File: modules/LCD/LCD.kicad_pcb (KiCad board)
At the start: 2 copper layers, 82.5 x 40.6 mm, 8 parts, among them J1 Conn_01x10_Male, J2 Conn_01x10_Male

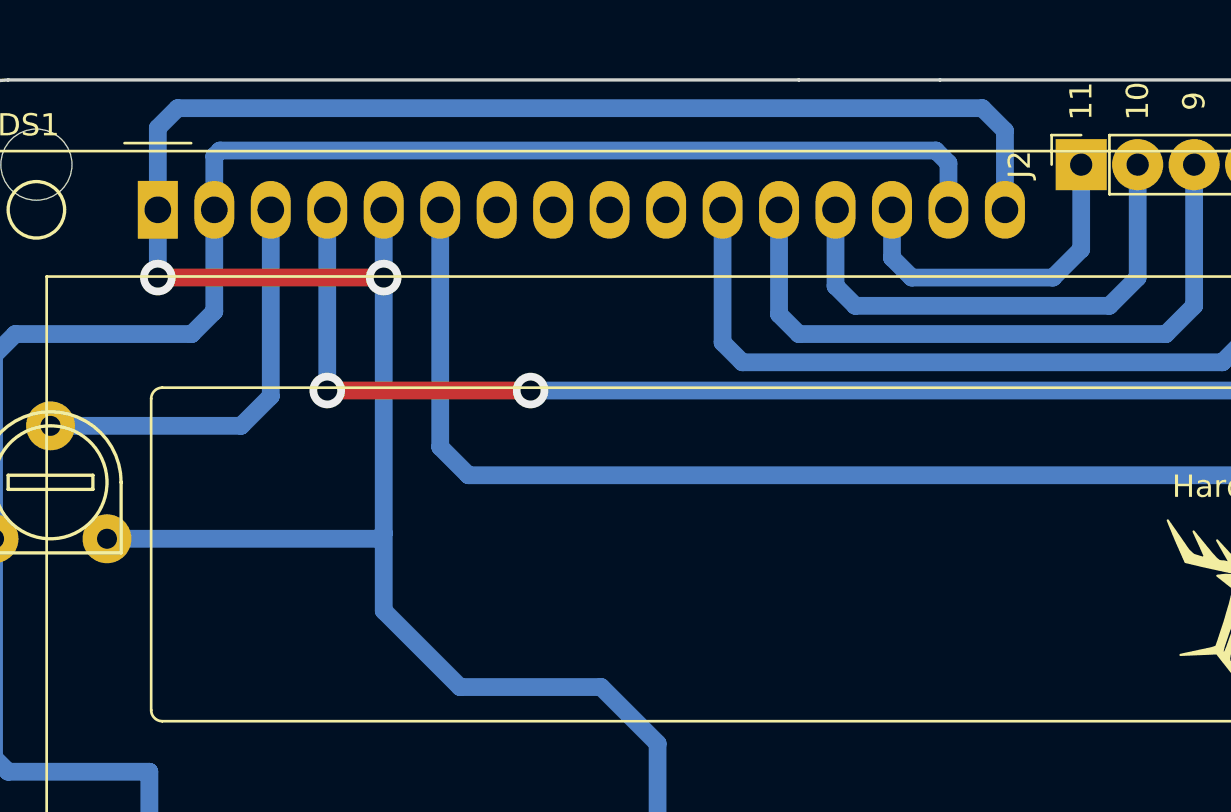
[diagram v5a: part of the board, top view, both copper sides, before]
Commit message: My LCD does not have LED resistor :( Add silk etc
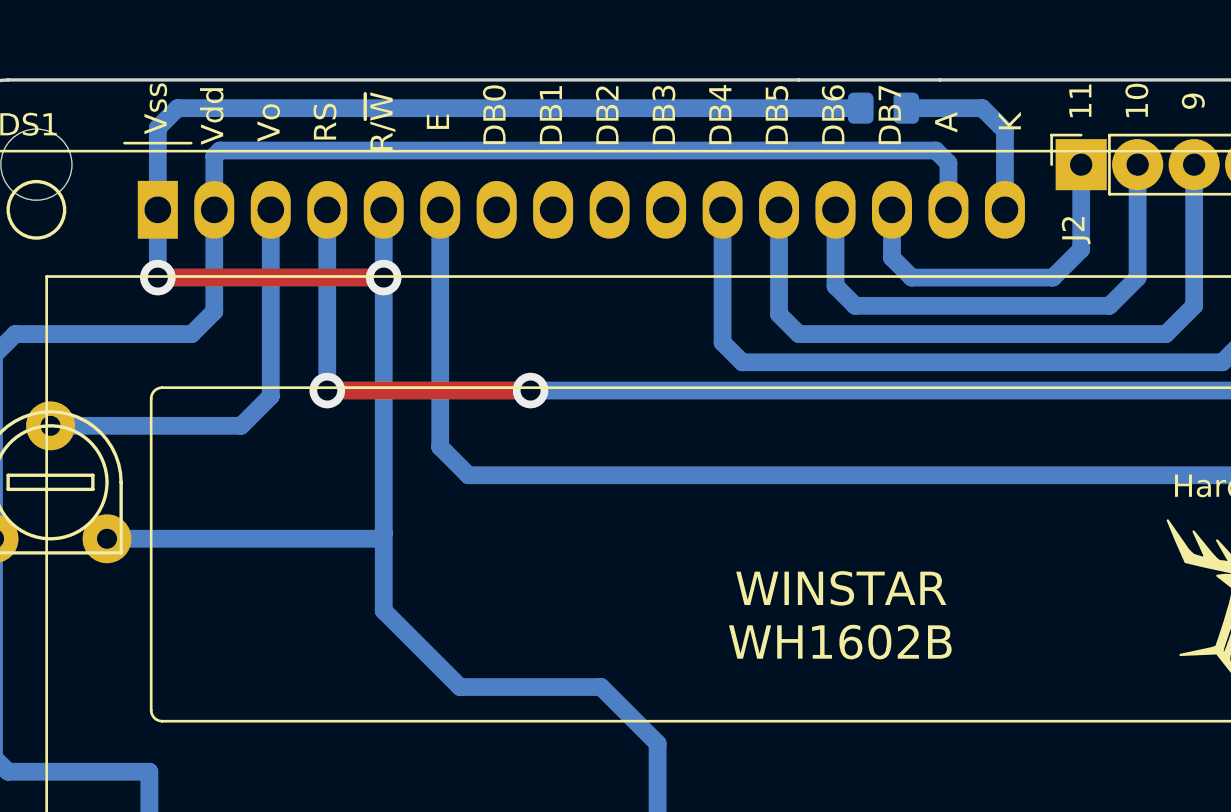
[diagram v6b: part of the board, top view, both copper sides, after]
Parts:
- added R1: 20, Resistor_SMD:R_0805_2012Metric_Pad1.15x1.40mm_HandSolder, B.Cu at (111.1, 26.7)
- DS1: value WC1602A -> WH1602B
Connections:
- DS1 pad 16: GND -> Net-(DS1-Pad16)
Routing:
- net GND: track 111.6 -> 101.2 mm
- net Net-(DS1-Pad16): track 0.00 -> 8.41 mm
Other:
- board text added: "A"
- board text added: "DB0"
- board text added: "DB1"
- board text added: "DB2"
- board text added: "DB3"
- board text added: "DB4"
- board text added: "DB5"
- board text added: "DB6"
- board text added: "DB7"
- board text added: "E"
- board text added: "K"
- board text added: "R/~W"
- board text added: "RS"
- board text added: "Vdd"
- board text added: "Vo"
- board text added: "Vss"
- board text added: "WINSTAR WH1602B"
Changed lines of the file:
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@@
   (general
     (thickness 1.6)
-    (drawings 37)
-    (tracks 74)
+    (drawings 54)
+    (tracks 75)
     (zones 0)
-    (modules 8)
-    (nets 26)
+    (modules 9)
+    (nets 27)
   )
   (page A4 portrait)
@@
   )
   (setup
-    (last_trace_width 0.25)
+    (last_trace_width 0.6)
     (user_trace_width 0.6)
     (user_trace_width 0.8)
@@
   (net 24 "Net-(DS1-Pad8)")
   (net 25 "Net-(DS1-Pad7)")
+  (net 26 "Net-(DS1-Pad16)")
   (net_class Default "Это класс цепей по умолчанию."
     (clearance 0.2)
@@
     (add_net GND)
     (add_net "Net-(DS1-Pad10)")
+    (add_net "Net-(DS1-Pad16)")
     (add_net "Net-(DS1-Pad3)")
     (add_net "Net-(DS1-Pad7)")
@@
     (descr "Through hole straight socket strip, 1x10, 2.54mm pitch, single row (from Kicad 4.0.7), script generated")
     (tags "Through hole socket strip THT 1x10 2.54mm single row")
-    (fp_text reference J2 (at 0 -2.77 90) (layer F.SilkS)
+    (fp_text reference J2 (at -2.8575 -0.3175 90) (layer F.SilkS)
       (effects (font (size 1 1) (thickness 0.15)))
     )
@@
       (effects (font (size 1 1) (thickness 0.15)))
     )
-    (fp_text value WC1602A (at -4.31 34.66) (layer F.Fab)
+    (fp_text value WH1602B (at -4.31 34.66) (layer F.Fab)
       (effects (font (size 1 1) (thickness 0.15)))
     )
@@
     (fp_circle (center 69.469 30.988) (end 70.231 32.004) (layer F.SilkS) (width 0.15))
     (pad 16 thru_hole oval (at 38.1 0) (size 1.8 2.6) (drill 1.2) (layers *.Cu *.Mask)
-      (net 10 GND))
+      (net 26 "Net-(DS1-Pad16)"))
     (pad 15 thru_hole oval (at 35.56 0) (size 1.8 2.6) (drill 1.2) (layers *.Cu *.Mask)
       (net 1 VCC))
@@
       (net 10 GND))
   )
+  (module Resistor_SMD:R_0805_2012Metric_Pad1.15x1.40mm_HandSolder (layer B.Cu)
+    (at 111.125 26.67 180)
+    (descr "Resistor SMD 0805 (2012 Metric), square (rectangular) end terminal, IPC_7351 nominal with elongated pad for handsoldering. (Body size source: https://docs.google.com/spreadsheets/d/1BsfQQcO9C6DZCsRaXUlFlo91Tg2WpOkGARC1WS5S8t0/edit?usp=sharing), generated with kicad-footprint-generator")
+    (tags "resistor handsolder")
+    (attr smd)
+    (fp_text reference R1 (at -3.175 0) (layer B.SilkS)
+      (effects (font (size 1 1) (thickness 0.15)) (justify mirror))
+    )
+    (fp_text value 20 (at 0 -1.65) (layer B.Fab)
+      (effects (font (size 1 1) (thickness 0.15)) (justify mirror))
+    )
+    (fp_line (start -1 -0.6) (end -1 0.6) (layer B.Fab) (width 0.1))
+    (fp_line (start -1 0.6) (end 1 0.6) (layer B.Fab) (width 0.1))
+    (fp_line (start 1 0.6) (end 1 -0.6) (layer B.Fab) (width 0.1))
+    (fp_line (start 1 -0.6) (end -1 -0.6) (layer B.Fab) (width 0.1))
+    (fp_line (start -0.261252 0.71) (end 0.261252 0.71) (layer B.SilkS) (width 0.12))
+    (fp_line (start -0.261252 -0.71) (end 0.261252 -0.71) (layer B.SilkS) (width 0.12))
+    (fp_line (start -1.85 -0.95) (end -1.85 0.95) (layer B.CrtYd) (width 0.05))
+    (fp_line (start -1.85 0.95) (end 1.85 0.95) (layer B.CrtYd) (width 0.05))
+    (fp_line (start 1.85 0.95) (end 1.85 -0.95) (layer B.CrtYd) (width 0.05))
+    (fp_line (start 1.85 -0.95) (end -1.85 -0.95) (layer B.CrtYd) (width 0.05))
+    (fp_text user %R (at 0 0) (layer B.Fab)
+      (effects (font (size 0.5 0.5) (thickness 0.08)) (justify mirror))
+    )
+    (pad 1 smd roundrect (at -1.025 0 180) (size 1.15 1.4) (layers B.Cu B.Paste B.Mask) (roundrect_rratio 0.217391)
+      (net 26 "Net-(DS1-Pad16)"))
+    (pad 2 smd roundrect (at 1.025 0 180) (size 1.15 1.4) (layers B.Cu B.Paste B.Mask) (roundrect_rratio 0.217391)
+      (net 10 GND))
+    (model ${KISYS3DMOD}/Resistor_SMD.3dshapes/R_0805_2012Metric.wrl
+      (at (xyz 0 0 0))
+      (scale (xyz 1 1 1))
+      (rotate (xyz 0 0 0))
+    )
+  )
+  (gr_text K (at 116.84 27.305 90) (layer F.SilkS)
+    (effects (font (size 1 1) (thickness 0.15)))
+  )
+  (gr_text A (at 113.9825 27.305 90) (layer F.SilkS)
+    (effects (font (size 1 1) (thickness 0.15)))
+  )
+  (gr_text DB7 (at 111.4425 26.9875 90) (layer F.SilkS)
+    (effects (font (size 1 1) (thickness 0.15)))
+  )
+  (gr_text DB6 (at 108.9025 26.9875 90) (layer F.SilkS)
+    (effects (font (size 1 1) (thickness 0.15)))
+  )
+  (gr_text DB5 (at 106.3625 26.9875 90) (layer F.SilkS)
+    (effects (font (size 1 1) (thickness 0.15)))
+  )
+  (gr_text DB4 (at 103.8225 26.9875 90) (layer F.SilkS)
+    (effects (font (size 1 1) (thickness 0.15)))
+  )
+  (gr_text DB3 (at 101.2825 26.9875 90) (layer F.SilkS)
+    (effects (font (size 1 1) (thickness 0.15)))
+  )
+  (gr_text DB2 (at 98.7425 26.9875 90) (layer F.SilkS)
+    (effects (font (size 1 1) (thickness 0.15)))
+  )
+  (gr_text DB1 (at 96.2025 26.9875 90) (layer F.SilkS)
+    (effects (font (size 1 1) (thickness 0.15)))
+  )
+  (gr_text DB0 (at 93.6625 26.9875 90) (layer F.SilkS)
+    (effects (font (size 1 1) (thickness 0.15)))
+  )
+  (gr_text E (at 91.1225 27.305 90) (layer F.SilkS)
+    (effects (font (size 1 1) (thickness 0.15)))
+  )
+  (gr_text R/~W (at 88.5825 27.305 90) (layer F.SilkS)
+    (effects (font (size 1 1) (thickness 0.15)))
+  )
+  (gr_text RS (at 86.0425 27.305 90) (layer F.SilkS)
+    (effects (font (size 1 1) (thickness 0.15)))
+  )
+  (gr_text Vo (at 83.5025 27.305 90) (layer F.SilkS)
+    (effects (font (size 1 1) (thickness 0.15)))
+  )
+  (gr_text Vdd (at 80.9625 26.9875 90) (layer F.SilkS)
+    (effects (font (size 1 1) (thickness 0.15)))
+  )
+  (gr_text Vss (at 78.4225 26.67 90) (layer F.SilkS)
+    (effects (font (size 1 1) (thickness 0.15)))
+  )
+  (gr_text "WINSTAR\nWH1602B" (at 109.22 49.53) (layer F.SilkS)
+    (effects (font (size 1.5 1.5) (thickness 0.2)))
+  )
   (gr_line (start 107.315 25.4) (end 113.665 25.4) (layer Edge.Cuts) (width 0.15))
   (gr_text c86590 (at 139.065 62.865) (layer B.Cu)
@@
   (segment (start 100.965 55.245) (end 100.965 62.23) (width 0.8) (layer B.Cu) (net 10))
   (segment (start 92.075 52.705) (end 98.425 52.705) (width 0.8) (layer B.Cu) (net 10))
-  (segment (start 116.586 27.686) (end 116.586 31.242) (width 0.8) (layer B.Cu) (net 10))
-  (segment (start 115.57 26.67) (end 116.586 27.686) (width 0.8) (layer B.Cu) (net 10))
-  (segment (start 79.375 26.67) (end 115.57 26.67) (width 0.8) (layer B.Cu) (net 10))
+  (segment (start 116.586 27.686) (end 116.586 31.242) (width 0.8) (layer B.Cu) (net 26))
+  (segment (start 115.57 26.67) (end 116.586 27.686) (width 0.8) (layer B.Cu) (net 26))
   (segment (start 78.486 31.242) (end 78.486 27.559) (width 0.8) (layer B.Cu) (net 10))
   (segment (start 78.486 27.559) (end 79.375 26.67) (width 0.8) (layer B.Cu) (net 10))
@@
   (segment (start 88.646 45.7835) (end 88.392 46.0375) (width 0.8) (layer B.Cu) (net 10))
   (segment (start 88.646 34.544) (end 88.646 45.7835) (width 0.8) (layer B.Cu) (net 10))
+  (segment (start 79.375 26.67) (end 110.1 26.67) (width 0.8) (layer B.Cu) (net 10))
   (segment (start 142.875 39.37) (end 142.875 29.21) (width 0.8) (layer B.Cu) (net 11))
   (segment (start 141.605 43.18) (end 142.875 41.91) (width 0.8) (layer B.Cu) (net 11))
@@
   (segment (start 83.566 39.624) (end 82.2325 40.9575) (width 0.8) (layer B.Cu) (net 21))
   (segment (start 96.266 31.242) (end 96.266 31.642) (width 0.6) (layer B.Cu) (net 24))
+  (segment (start 115.57 26.67) (end 112.15 26.67) (width 0.8) (layer B.Cu) (net 26))
 )

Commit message: LED polishing
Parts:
- RV1: footprint CommonLibrary:pot-5x5 -> Potentiometer_THT:Potentiometer_ACP_CA6-H2,5_Horizontal
- moved RV1 0.90 mm to (73.0, 42.9), turned to 0 degrees
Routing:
- net GND: track 101.2 -> 104.2 mm
- net Net-(DS1-Pad3): track 18.8 -> 20.8 mm
- net VCC: track 84.2 -> 86.1 mm
- net (no net): vias 0 -> 10
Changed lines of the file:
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@@
     (thickness 1.6)
     (drawings 54)
-    (tracks 75)
+    (tracks 87)
     (zones 0)
     (modules 9)
@@
   )
   (setup
-    (last_trace_width 0.6)
+    (last_trace_width 0.8)
     (user_trace_width 0.6)
     (user_trace_width 0.8)
@@
     (via_min_drill 0.3)
     (user_via 1.6 0.9)
+    (user_via 2.2 0.9)
     (uvia_size 0.3)
     (uvia_drill 0.1)
@@
     )
   )
-  (module CommonLibrary:pot-5x5 (layer F.Cu)
-    (at 73.66 43.4975 270)
-    (fp_text reference RV1 (at 0.635 4.445 90) (layer F.SilkS)
-      (effects (font (size 1 1) (thickness 0.15)))
-    )
-    (fp_text value R_POT (at 0 -0.5 90) (layer F.Fab)
-      (effects (font (size 1 1) (thickness 0.15)))
-    )
-    (fp_circle (center 0 0) (end 0 -2.54) (layer F.SilkS) (width 0.15))
-    (fp_arc (start 0 0) (end 0 -3.175) (angle -180) (layer F.SilkS) (width 0.15))
-    (fp_line (start 0 -3.175) (end 3.175 -3.175) (layer F.SilkS) (width 0.15))
-    (fp_line (start 3.175 -3.175) (end 3.175 3.175) (layer F.SilkS) (width 0.15))
-    (fp_line (start 3.175 3.175) (end 0 3.175) (layer F.SilkS) (width 0.15))
-    (fp_line (start -0.3175 -1.905) (end 0.3175 -1.905) (layer F.SilkS) (width 0.15))
-    (fp_line (start 0.3175 -1.905) (end 0.3175 1.905) (layer F.SilkS) (width 0.15))
-    (fp_line (start 0.3175 1.905) (end -0.3175 1.905) (layer F.SilkS) (width 0.15))
-    (fp_line (start -0.3175 1.905) (end -0.3175 -1.905) (layer F.SilkS) (width 0.15))
-    (pad 2 thru_hole circle (at -2.54 0 270) (size 2.2 2.2) (drill 0.9) (layers *.Cu *.Mask)
-      (net 21 "Net-(DS1-Pad3)"))
-    (pad 1 thru_hole circle (at 2.54 2.54 270) (size 2.2 2.2) (drill 0.9) (layers *.Cu *.Mask)
-      (net 1 VCC))
-    (pad 3 thru_hole circle (at 2.54 -2.54 270) (size 2.2 2.2) (drill 0.9) (layers *.Cu *.Mask)
-      (net 10 GND))
-  )
   (module Resistor_SMD:R_0805_2012Metric_Pad1.15x1.40mm_HandSolder (layer B.Cu)
     (at 111.125 26.67 180)
@@
     )
   )
+  (module Potentiometer_THT:Potentiometer_ACP_CA6-H2,5_Horizontal (layer F.Cu)
+    (at 73.025 42.8625)
+    (descr "Potentiometer, horizontal, ACP CA6-H2,5, http://www.acptechnologies.com/wp-content/uploads/2017/06/01-ACP-CA6.pdf")
+    (tags "Potentiometer horizontal ACP CA6-H2,5")
+    (fp_text reference RV1 (at 0 -2.06) (layer F.SilkS)
+      (effects (font (size 1 1) (thickness 0.15)))
+    )
+    (fp_text value R_POT (at 0 7.06) (layer F.Fab)
+      (effects (font (size 1 1) (thickness 0.15)))
+    )
+    (fp_line (start 3.5 -0.65) (end 3.5 5.65) (layer F.Fab) (width 0.1))
+    (fp_line (start 3.5 5.65) (end 0 5.65) (layer F.Fab) (width 0.1))
+    (fp_line (start 0 5.65) (end 0 -0.65) (layer F.Fab) (width 0.1))
+    (fp_line (start 0 -0.65) (end 3.5 -0.65) (layer F.Fab) (width 0.1))
+    (fp_line (start 0 1.5) (end 0 3.5) (layer F.Fab) (width 0.1))
+    (fp_line (start 0 3.5) (end 3.5 3.5) (layer F.Fab) (width 0.1))
+    (fp_line (start 3.5 3.5) (end 3.5 1.5) (layer F.Fab) (width 0.1))
+    (fp_line (start 3.5 1.5) (end 0 1.5) (layer F.Fab) (width 0.1))
+    (fp_line (start 0.925 -0.77) (end 3.62 -0.77) (layer F.SilkS) (width 0.12))
+    (fp_line (start 0.925 5.77) (end 3.62 5.77) (layer F.SilkS) (width 0.12))
+    (fp_line (start 3.62 -0.77) (end 3.62 5.77) (layer F.SilkS) (width 0.12))
+    (fp_line (start -0.121 1.066) (end -0.121 3.935) (layer F.SilkS) (width 0.12))
+    (fp_line (start -0.121 1.38) (end 3.62 1.38) (layer F.SilkS) (width 0.12))
+    (fp_line (start -0.121 3.62) (end 3.62 3.62) (layer F.SilkS) (width 0.12))
+    (fp_line (start -0.121 1.38) (end -0.121 3.62) (layer F.SilkS) (width 0.12))
+    (fp_line (start 3.62 1.38) (end 3.62 3.62) (layer F.SilkS) (width 0.12))
+    (fp_line (start -1.1 -1.1) (end -1.1 6.1) (layer F.CrtYd) (width 0.05))
+    (fp_line (start -1.1 6.1) (end 3.75 6.1) (layer F.CrtYd) (width 0.05))
+    (fp_line (start 3.75 6.1) (end 3.75 -1.1) (layer F.CrtYd) (width 0.05))
+    (fp_line (start 3.75 -1.1) (end -1.1 -1.1) (layer F.CrtYd) (width 0.05))
+    (fp_text user %R (at 1.75 2.5) (layer F.Fab)
+      (effects (font (size 0.78 0.78) (thickness 0.15)))
+    )
+    (pad 3 thru_hole circle (at 0 5) (size 1.62 1.62) (drill 0.9) (layers *.Cu *.Mask)
+      (net 10 GND))
+    (pad 2 thru_hole circle (at 2.5 2.5) (size 1.62 1.62) (drill 0.9) (layers *.Cu *.Mask)
+      (net 21 "Net-(DS1-Pad3)"))
+    (pad 1 thru_hole circle (at 0 0) (size 1.62 1.62) (drill 0.9) (layers *.Cu *.Mask)
+      (net 1 VCC))
+    (model ${KISYS3DMOD}/Potentiometer_THT.3dshapes/Potentiometer_ACP_CA6-H2,5_Horizontal.wrl
+      (at (xyz 0 0 0))
+      (scale (xyz 1 1 1))
+      (rotate (xyz 0 0 0))
+    )
+  )
   (gr_text K (at 116.84 27.305 90) (layer F.SilkS)
     (effects (font (size 1 1) (thickness 0.15)))
@@
   )
   (gr_line (start 107.315 25.4) (end 113.665 25.4) (layer Edge.Cuts) (width 0.15))
-  (gr_text c86590 (at 139.065 62.865) (layer B.Cu)
+  (gr_text c86590 (at 135.89 56.515) (layer B.Cu)
     (effects (font (size 1 1) (thickness 0.2)) (justify mirror))
   )
-  (gr_text v2 (at 131.1275 62.5475) (layer B.Cu)
+  (gr_text v2 (at 127.9525 56.1975) (layer B.Cu)
     (effects (font (size 1.5 1.5) (thickness 0.3)) (justify mirror))
   )
-  (gr_text 26.04.2020 (at 122.2375 62.865) (layer B.Cu)
+  (gr_text 26.04.2020 (at 119.0625 56.515) (layer B.Cu)
     (effects (font (size 1 1) (thickness 0.2)) (justify mirror))
   )
@@
   (segment (start 78.105 64.135) (end 78.105 65.405) (width 0.25) (layer B.Cu) (net 0))
   (segment (start 77.47 64.77) (end 78.74 64.77) (width 0.25) (layer B.Cu) (net 0))
+  (via (at 120.015 62.23) (size 2.2) (drill 0.9) (layers F.Cu B.Cu) (net 0))
+  (via (at 122.555 62.23) (size 2.2) (drill 0.9) (layers F.Cu B.Cu) (net 0))
+  (via (at 125.095 62.23) (size 2.2) (drill 0.9) (layers F.Cu B.Cu) (net 0))
+  (via (at 127.635 62.23) (size 2.2) (drill 0.9) (layers F.Cu B.Cu) (net 0))
+  (via (at 130.175 62.23) (size 2.2) (drill 0.9) (layers F.Cu B.Cu) (net 0))
+  (via (at 132.715 62.23) (size 2.2) (drill 0.9) (layers F.Cu B.Cu) (net 0))
+  (via (at 135.255 62.23) (size 2.2) (drill 0.9) (layers F.Cu B.Cu) (net 0))
+  (via (at 137.795 62.23) (size 2.2) (drill 0.9) (layers F.Cu B.Cu) (net 0))
+  (via (at 140.335 62.23) (size 2.2) (drill 0.9) (layers F.Cu B.Cu) (net 0))
+  (via (at 142.875 62.23) (size 2.2) (drill 0.9) (layers F.Cu B.Cu) (net 0))
   (segment (start 81.026 31.242) (end 81.026 28.829) (width 0.8) (layer B.Cu) (net 1))
   (segment (start 81.026 28.829) (end 81.28 28.575) (width 0.8) (layer B.Cu) (net 1))
@@
   (segment (start 71.12 37.7825) (end 72.0725 36.83) (width 0.8) (layer B.Cu) (net 1))
   (segment (start 72.0725 36.83) (end 80.01 36.83) (width 0.8) (layer B.Cu) (net 1))
-  (segment (start 71.12 55.88) (end 71.12 37.7825) (width 0.8) (layer B.Cu) (net 1))
+  (segment (start 71.12 55.88) (end 71.12 42.8625) (width 0.8) (layer B.Cu) (net 1))
+  (segment (start 73.025 42.8625) (end 71.12 42.8625) (width 0.8) (layer B.Cu) (net 1))
+  (segment (start 71.12 42.8625) (end 71.12 37.7825) (width 0.8) (layer B.Cu) (net 1))
   (segment (start 88.646 36.576) (end 88.646 36.576) (width 0.8) (layer B.Cu) (net 10))
   (segment (start 88.646 31.242) (end 88.646 34.544) (width 0.8) (layer B.Cu) (net 10))
@@
   (segment (start 100.965 55.245) (end 100.965 62.23) (width 0.8) (layer B.Cu) (net 10))
   (segment (start 92.075 52.705) (end 98.425 52.705) (width 0.8) (layer B.Cu) (net 10))
-  (segment (start 116.586 27.686) (end 116.586 31.242) (width 0.8) (layer B.Cu) (net 26))
-  (segment (start 115.57 26.67) (end 116.586 27.686) (width 0.8) (layer B.Cu) (net 26))
   (segment (start 78.486 31.242) (end 78.486 27.559) (width 0.8) (layer B.Cu) (net 10))
   (segment (start 78.486 27.559) (end 79.375 26.67) (width 0.8) (layer B.Cu) (net 10))
@@
   (via (at 78.486 34.29) (size 1.6) (drill 0.9) (layers F.Cu B.Cu) (net 10))
   (segment (start 78.486 34.29) (end 88.646 34.29) (width 0.8) (layer F.Cu) (net 10))
-  (segment (start 88.392 46.0375) (end 76.2 46.0375) (width 0.8) (layer B.Cu) (net 10))
   (segment (start 88.646 45.7835) (end 88.646 49.276) (width 0.8) (layer B.Cu) (net 10))
-  (segment (start 88.646 45.7835) (end 88.392 46.0375) (width 0.8) (layer B.Cu) (net 10))
   (segment (start 88.646 34.544) (end 88.646 45.7835) (width 0.8) (layer B.Cu) (net 10))
   (segment (start 79.375 26.67) (end 110.1 26.67) (width 0.8) (layer B.Cu) (net 10))
+  (segment (start 73.025 47.8625) (end 88.646 47.8625) (width 0.8) (layer B.Cu) (net 10))
   (segment (start 142.875 39.37) (end 142.875 29.21) (width 0.8) (layer B.Cu) (net 11))
   (segment (start 141.605 43.18) (end 142.875 41.91) (width 0.8) (layer B.Cu) (net 11))
@@
   (segment (start 112.395 34.29) (end 118.745 34.29) (width 0.8) (layer B.Cu) (net 20))
   (segment (start 83.566 31.242) (end 83.566 39.624) (width 0.8) (layer B.Cu) (net 21))
-  (segment (start 82.2325 40.9575) (end 73.66 40.9575) (width 0.8) (layer B.Cu) (net 21))
-  (segment (start 83.566 39.624) (end 82.2325 40.9575) (width 0.8) (layer B.Cu) (net 21))
+  (segment (start 75.525 45.3625) (end 81.32 45.3625) (width 0.8) (layer B.Cu) (net 21))
+  (segment (start 83.566 43.1165) (end 83.566 39.624) (width 0.8) (layer B.Cu) (net 21))
+  (segment (start 81.32 45.3625) (end 83.566 43.1165) (width 0.8) (layer B.Cu) (net 21))
   (segment (start 96.266 31.242) (end 96.266 31.642) (width 0.6) (layer B.Cu) (net 24))
+  (segment (start 116.586 27.686) (end 116.586 31.242) (width 0.8) (layer B.Cu) (net 26))
+  (segment (start 115.57 26.67) (end 116.586 27.686) (width 0.8) (layer B.Cu) (net 26))
   (segment (start 115.57 26.67) (end 112.15 26.67) (width 0.8) (layer B.Cu) (net 26))
 )

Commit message: Update hash
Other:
- board text added: "16.05.2020"
- board text added: "64baef"
- board text removed: "26.04.2020"
- board text removed: "c86590"
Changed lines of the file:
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@@
   )
   (setup
-    (last_trace_width 0.8)
+    (last_trace_width 0.25)
     (user_trace_width 0.6)
     (user_trace_width 0.8)
@@
   )
   (gr_line (start 107.315 25.4) (end 113.665 25.4) (layer Edge.Cuts) (width 0.15))
-  (gr_text c86590 (at 135.89 56.515) (layer B.Cu)
+  (gr_text 64baef (at 135.89 56.515) (layer B.Cu)
     (effects (font (size 1 1) (thickness 0.2)) (justify mirror))
   )
@@
     (effects (font (size 1.5 1.5) (thickness 0.3)) (justify mirror))
   )
-  (gr_text 26.04.2020 (at 119.0625 56.515) (layer B.Cu)
+  (gr_text 16.05.2020 (at 119.0625 56.515) (layer B.Cu)
     (effects (font (size 1 1) (thickness 0.2)) (justify mirror))
   )
